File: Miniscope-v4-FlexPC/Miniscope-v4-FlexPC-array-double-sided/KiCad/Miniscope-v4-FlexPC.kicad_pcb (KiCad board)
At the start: 2 copper layers, 25.2 x 23.5 mm, 7 parts, among them J1 Conn_01x20, J2 Conn_01x20, J3 Conn_01x05, J4 Conn_01x05, J5 Conn_01x14, J6 Conn_01x14

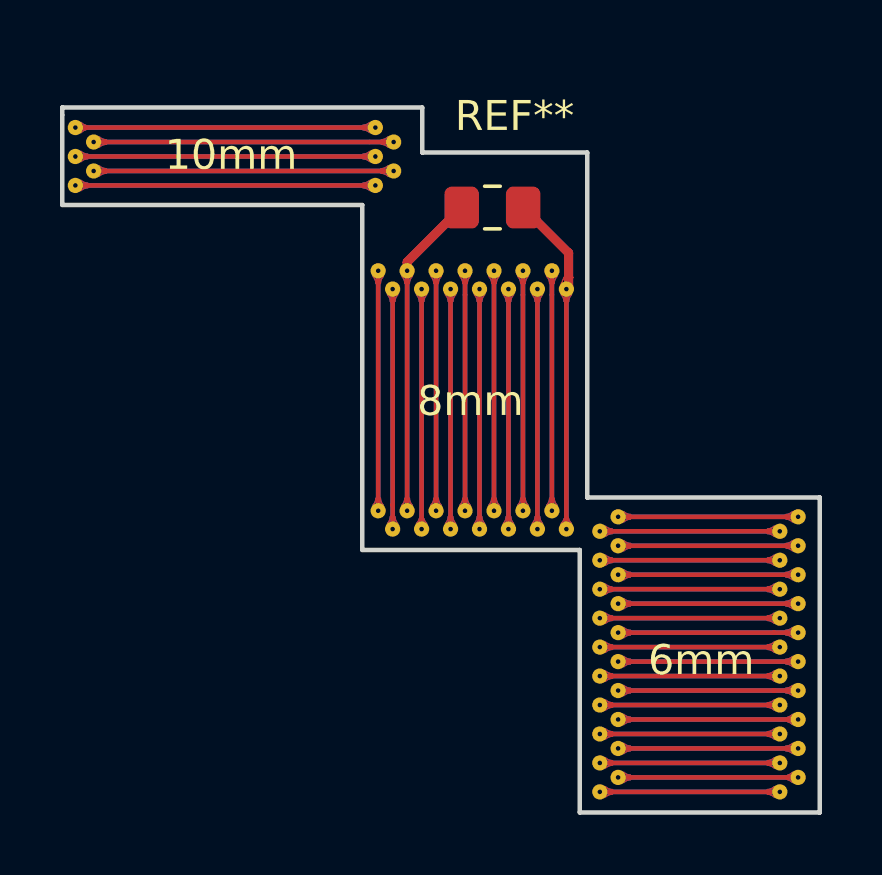
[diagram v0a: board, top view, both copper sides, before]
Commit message: Add I2C buffer to flexPC for V4. Ordered on 10/11/2019
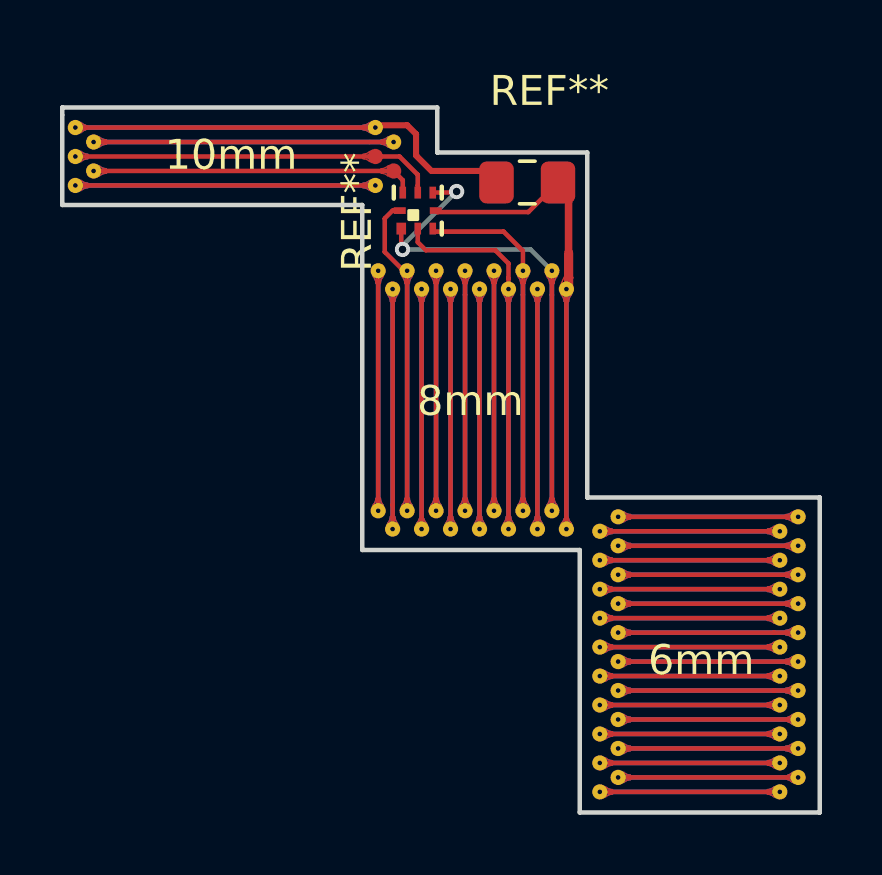
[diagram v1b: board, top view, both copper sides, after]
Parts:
- added REF**: XQFN8, .Package_QFN:XQFN8, F.Cu at (28.6, 18.2)
- moved REF** 1.43 mm to (32.2, 17.2)
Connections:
- REF** pad 1: Net-(J5-Pad3) -> Net-(J3-Pad5)
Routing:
- net Net-(J5-Pad13): track 16.0 -> 25.5 mm, vias 0 -> 2
- net Net-(J3-Pad2): track 20.0 -> 10.9 mm
- net Net-(J3-Pad3): track 20.0 -> 12.4 mm
- net Net-(J3-Pad5): track 20.0 -> 25.3 mm
- net Net-(J5-Pad14): track 19.4 -> 24.2 mm
- net Net-(J5-Pad10): track 16.0 -> 20.5 mm
- net Net-(J5-Pad11): track 16.0 -> 19.9 mm
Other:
- outline, holes or cut-outs redrawn
